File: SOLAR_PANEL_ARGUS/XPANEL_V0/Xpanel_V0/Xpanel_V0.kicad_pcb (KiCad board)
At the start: 8 copper layers, 82.6 x 98 mm, 45 parts, among them J1 0530470810, Q1 BSS138, Q2 BSS138, Q3 MBT2222ADW1T1, Q4 BSS138, Q5 BSS138, Q6 MBT2222ADW1T1, U1 DRV8830DGQ

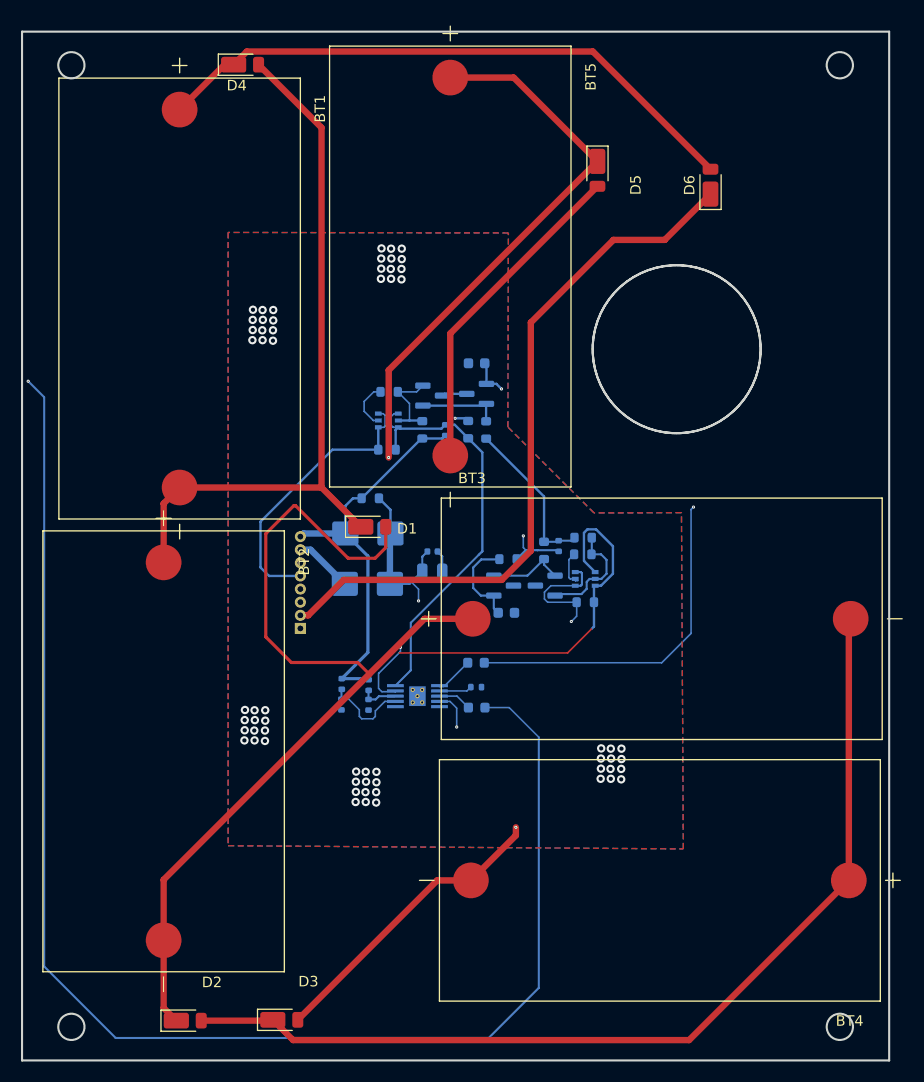
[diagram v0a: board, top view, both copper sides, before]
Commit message: Finished 2 coil layers of XPanel_V0 board
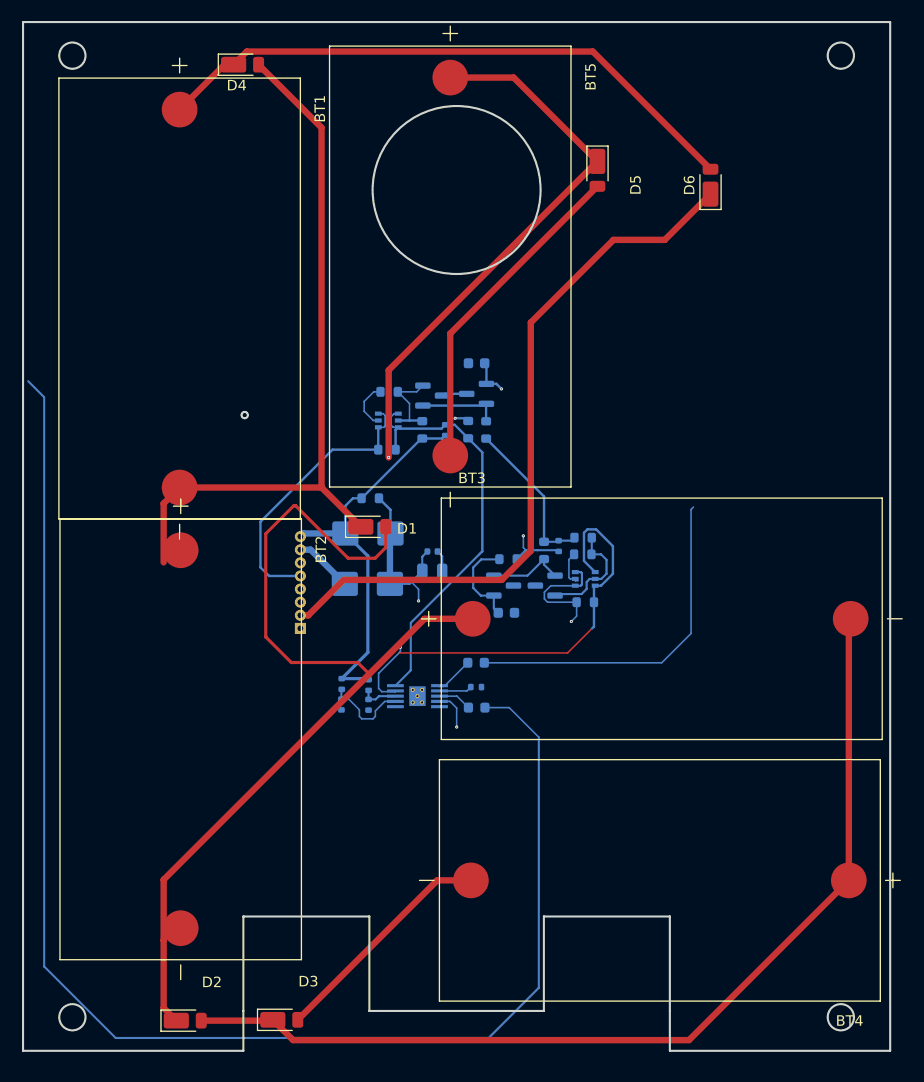
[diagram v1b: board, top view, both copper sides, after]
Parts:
- moved BT2 1.99 mm to (133.5, 114.7)
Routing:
- net /coils: track 80669.2 -> 82106.1 mm, vias 9 -> 4
- net Net-(D3-A): track 122.8 -> 75.8 mm, vias 2 -> 1
- net GND: vias 60 -> 0
- removed copper zone on B.Cu, net GND
- removed copper zone on F.Cu, net GND
- removed copper zone on In1.Cu, net GND
- removed copper zone on In2.Cu, net GND
- removed copper zone on In3.Cu, net GND
- removed copper zone on In4.Cu, net GND
- removed copper zone on In5.Cu, net GND
- removed copper zone on In6.Cu, net GND
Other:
- outline, holes or cut-outs redrawn

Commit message: Made first 2 layers identical for XPANEL_V0 Board
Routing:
- net /coils: track 82106.1 -> 87634.7 mm, vias 4 -> 11

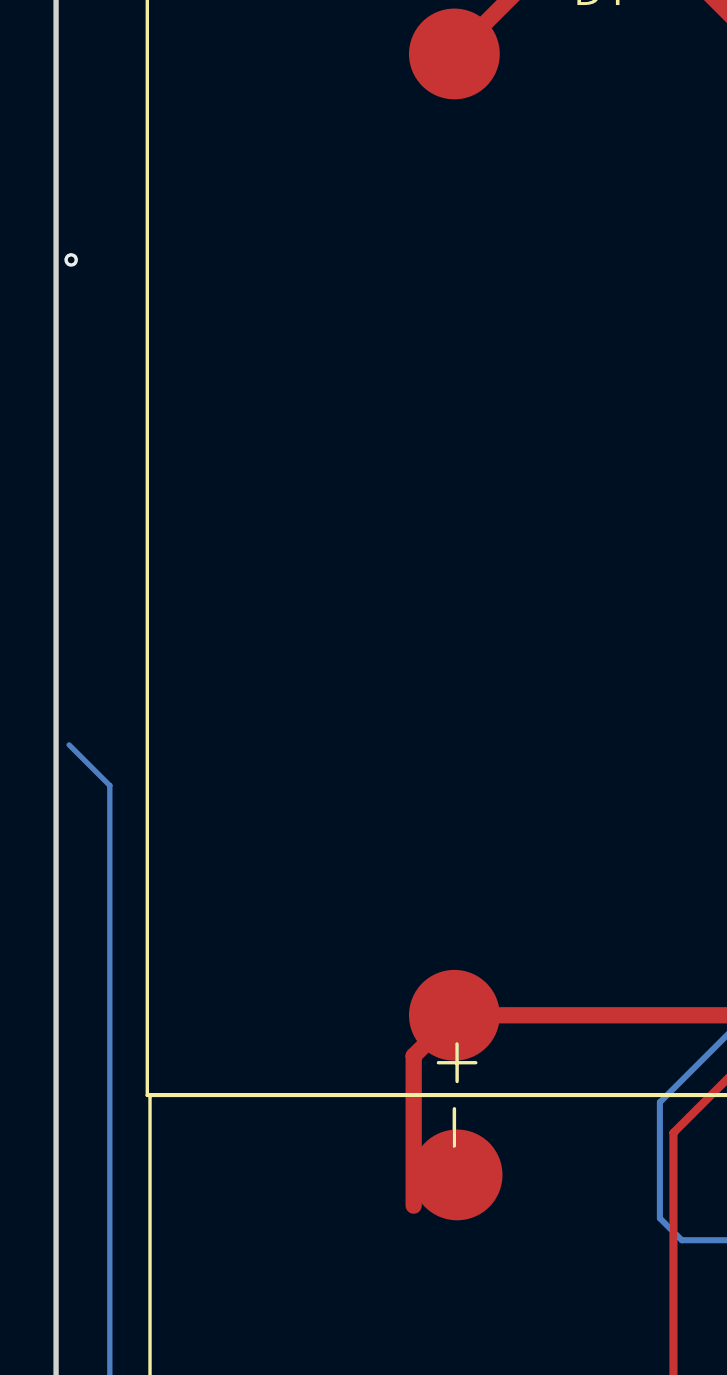
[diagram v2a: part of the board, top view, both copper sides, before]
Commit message: Finished 6 Layers of colis for XPANELV0 Board, but needs validation
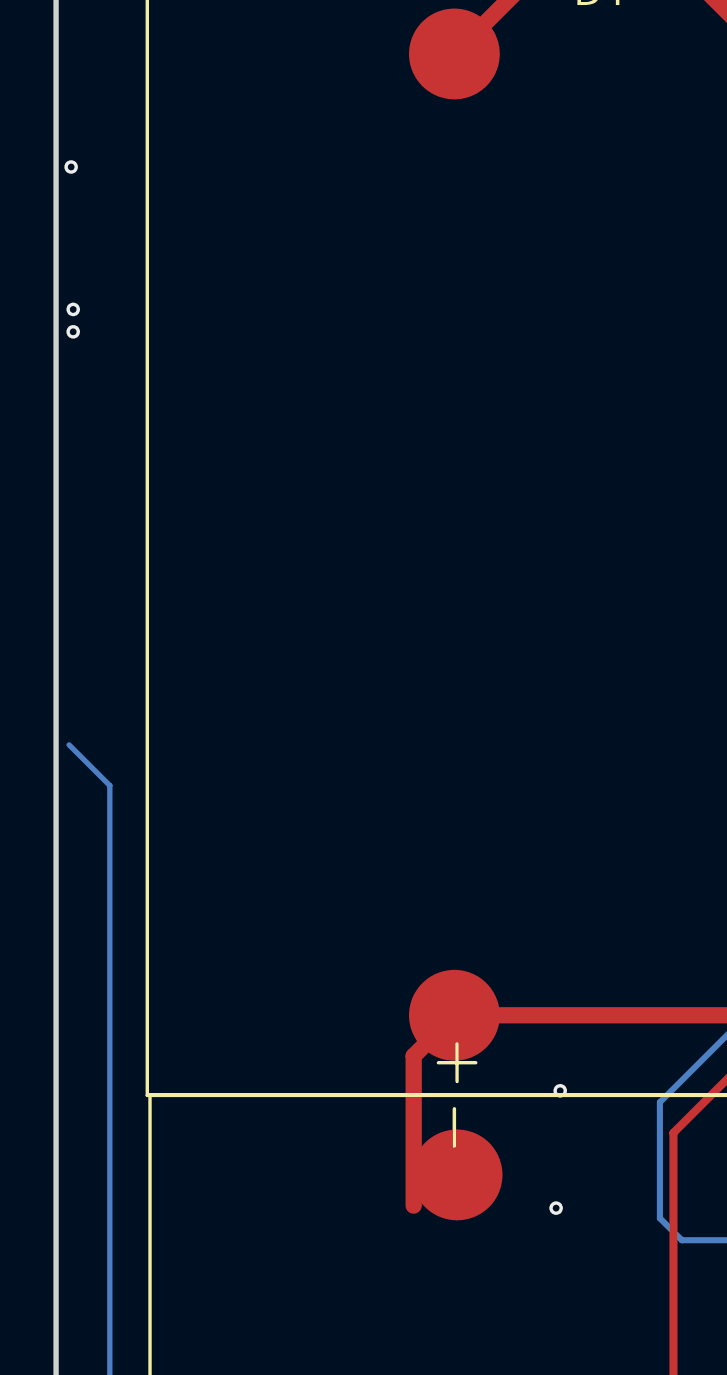
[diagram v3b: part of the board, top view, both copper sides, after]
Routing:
- net /coils: track 87634.7 -> 100740.8 mm, vias 11 -> 12
- net SDA1_b4iso: track 38.6 -> 11.5 mm
- net SDA: track 68.9 -> 49.6 mm
- net Net-(D7-K): track 33.6 -> 20.1 mm
- net Net-(Q2-G): track 10.7 -> 5.02 mm

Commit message: made changes
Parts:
- removed BT1, BT2, BT3, BT4, BT5: SM141K06L, SM141K06L:SOLAR_SM141K06L
- removed D1, D2, D3, D4, D5, D6: SBD, Diode_SMD:D_PowerDI-123
- removed J1: 0530470810, 0530470810:MOLEX_0530470810
- added B1: KXOB25-05X3F-TR, CHIP2_KXOB25-05X3F-TR_AAR:CHIP2_KXOB25-05X3F-TR_AAR, F.Cu at (137.7, 52.0)
- added B10: KXOB25-05X3F-TR, CHIP2_KXOB25-05X3F-TR_AAR:CHIP2_KXOB25-05X3F-TR_AAR, F.Cu at (147.5, 126.9)
- added B11: KXOB25-05X3F-TR, CHIP2_KXOB25-05X3F-TR_AAR:CHIP2_KXOB25-05X3F-TR_AAR, F.Cu at (188.6, 114.9)
- added B12: KXOB25-05X3F-TR, CHIP2_KXOB25-05X3F-TR_AAR:CHIP2_KXOB25-05X3F-TR_AAR, F.Cu at (189.1, 132.3)
- added B2: KXOB25-05X3F-TR, CHIP2_KXOB25-05X3F-TR_AAR:CHIP2_KXOB25-05X3F-TR_AAR, F.Cu at (133.0, 61.7)
- added B3: KXOB25-05X3F-TR, CHIP2_KXOB25-05X3F-TR_AAR:CHIP2_KXOB25-05X3F-TR_AAR, F.Cu at (159.4, 117.9)
- added B4: KXOB25-05X3F-TR, CHIP2_KXOB25-05X3F-TR_AAR:CHIP2_KXOB25-05X3F-TR_AAR, F.Cu at (172.3, 126.8)
- added B5: KXOB25-05X3F-TR, CHIP2_KXOB25-05X3F-TR_AAR:CHIP2_KXOB25-05X3F-TR_AAR, F.Cu at (196.0, 85.5)
- added B6: KXOB25-05X3F-TR, CHIP2_KXOB25-05X3F-TR_AAR:CHIP2_KXOB25-05X3F-TR_AAR, F.Cu at (188.1, 61.4)
- added B7: KXOB25-05X3F-TR, CHIP2_KXOB25-05X3F-TR_AAR:CHIP2_KXOB25-05X3F-TR_AAR, F.Cu at (179.9, 51.8)
- added B8: KXOB25-05X3F-TR, CHIP2_KXOB25-05X3F-TR_AAR:CHIP2_KXOB25-05X3F-TR_AAR, F.Cu at (131.2, 114.4)
- added B9: KXOB25-05X3F-TR, CHIP2_KXOB25-05X3F-TR_AAR:CHIP2_KXOB25-05X3F-TR_AAR, F.Cu at (130.7, 131.7)
- added J2: F3311A7H121014E200, F3311A7H121008E200:F3311A7H121014E200, B.Cu at (179.3, 100.2)
- added JP1: ~, SparkFun-Jumper:SMT-JUMPER_3_NO_NO-SILK, F.Cu at (195.5, 108.3)
- added JP2: ~, SparkFun-Jumper:SMT-JUMPER_3_NO_NO-SILK, F.Cu at (195.6, 105.5)
- added JP3: ~, SparkFun-Jumper:SMT-JUMPER_3_NO_NO-SILK, F.Cu at (173.2, 113.5)
- added JP4: ~, SparkFun-Jumper:SMT-JUMPER_3_NO_NO-SILK, F.Cu at (173.2, 115.7)
- added Q7: KXOB201K04F-TR, KXOB201K04TF-TR:TRAN_KXOB201K04F-TR_AAR, F.Cu at (179.3, 87.8)
- added Q8: KXOB201K04F-TR, KXOB201K04TF-TR:TRAN_KXOB201K04F-TR_AAR, F.Cu at (155.1, 92.0)
- added Q9: KXOB201K04F-TR, KXOB201K04TF-TR:TRAN_KXOB201K04F-TR_AAR, F.Cu at (130.8, 87.9)
- added U2: OPT4001DTST, OPT4001DTST:DTS0008A-MFG, F.Cu at (195.9, 102.6)
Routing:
- net Net-(D2-A): track 93.8 -> 0.00 mm
- net Net-(D1-A): track 91.8 -> 0.00 mm
- net Net-(D3-A): track 75.8 -> 0.00 mm, vias 1 -> 0
- net Net-(D1-K): track 69.3 -> 0.00 mm
- net /VSOLAR: track 68.4 -> 0.00 mm
- net /coils: track 100740.8 -> 100674.6 mm, vias 12 -> 10
- net Net-(D4-K): track 57.5 -> 0.00 mm
- net GND: track 35.9 -> 4.43 mm
- net SDA: track 49.6 -> 30.3 mm
